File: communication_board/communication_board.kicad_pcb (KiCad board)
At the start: 2 copper layers, 23 parts, among them J1 Conn_01x04_Socket, J2 Conn_01x04_Socket, U1 FE1.1s, U2 FT232RL, Y1 Crystal

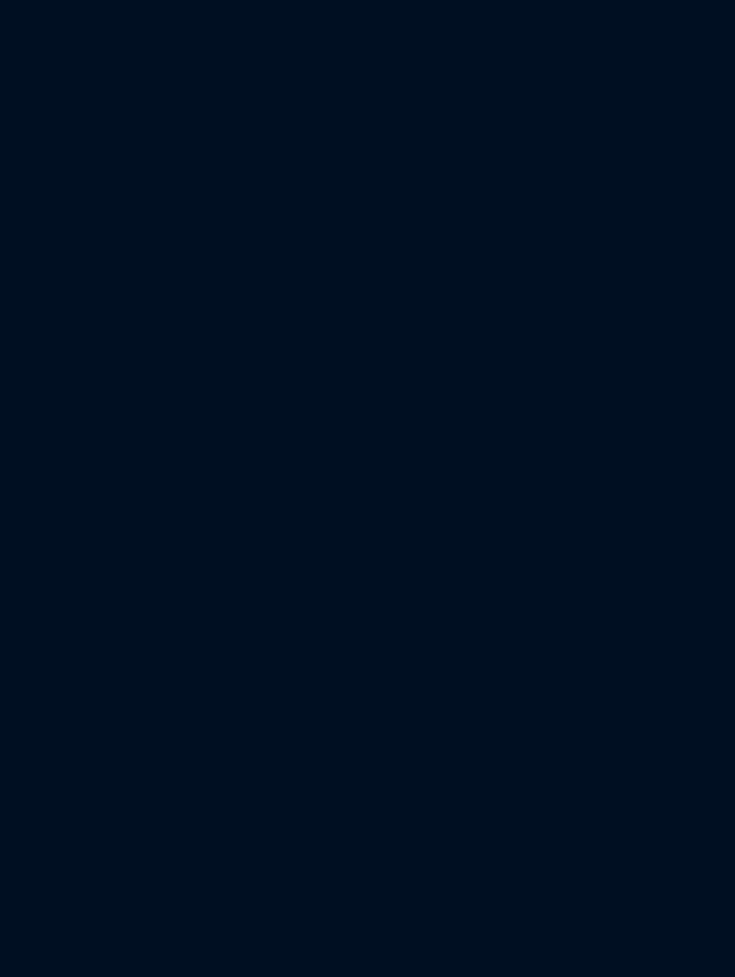
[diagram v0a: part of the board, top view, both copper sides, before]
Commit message: motors conversor almost ready for test
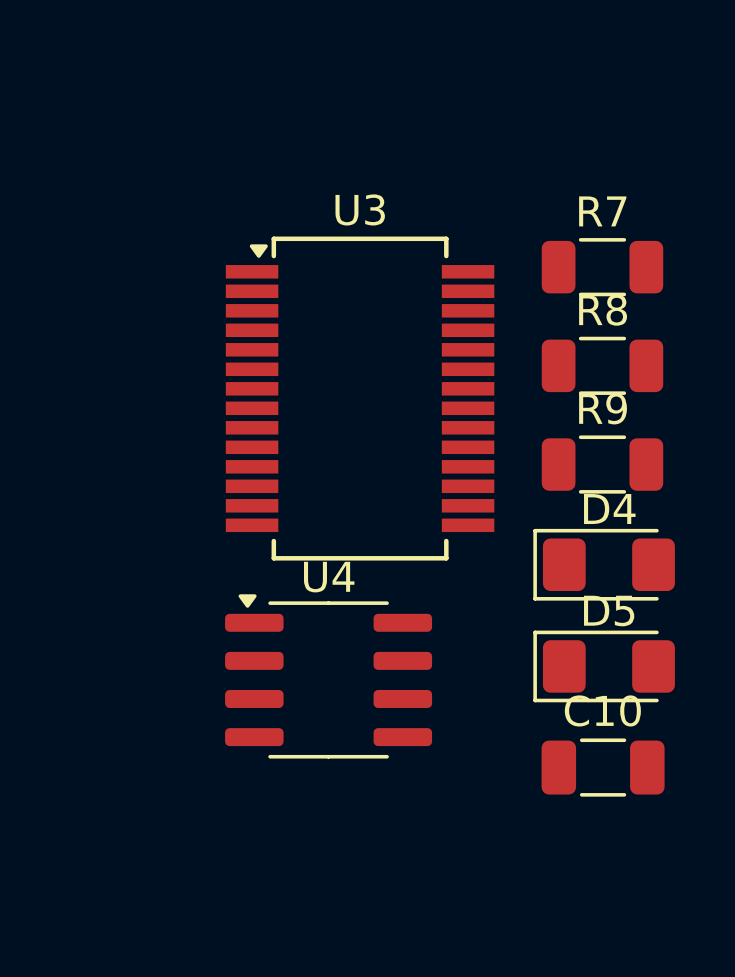
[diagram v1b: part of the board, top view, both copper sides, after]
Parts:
- added C10: 0.1uF, Capacitor_SMD:C_1206_3216Metric, F.Cu at (195.5, 76.5)
- added D4: IMU_TX, LED_SMD:LED_1206_3216Metric_Pad1.42x1.75mm_HandSolder, F.Cu at (195.7, 69.7)
- added D5: IMU_RX, LED_SMD:LED_1206_3216Metric_Pad1.42x1.75mm_HandSolder, F.Cu at (195.7, 73.1)
- added R7: 10K, Resistor_SMD:R_1206_3216Metric, F.Cu at (195.5, 59.8)
- added R8: 270, Resistor_SMD:R_1206_3216Metric, F.Cu at (195.5, 63.1)
- added R9: 270, Resistor_SMD:R_1206_3216Metric, F.Cu at (195.5, 66.4)
- added U3: FT232RL, Package_SO:SSOP-28_5.3x10.2mm_P0.65mm, F.Cu at (187.4, 64.2)
- added U4: MAX485E, Package_SO:SOIC-8_3.9x4.9mm_P1.27mm, F.Cu at (186.4, 73.6)
- R2: value 1K -> 330
- R3, R4: value 1k -> 330
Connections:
- net IMU_USB_D+_1 renamed IMU_USB_D+
- net IMU_USB_D-_1 renamed IMU_USB_D-
- U1 pad 8: HUB_USB_D-_2 -> MOTORS_USB_D-
- U1 pad 9: HUB_USB_D+_2 -> MOTORS_USB_D+
- U2 pad 22: unconnected-(U2-CBUS1-Pad22) -> Net-(D5-K)
- U2 pad 23: unconnected-(U2-CBUS0-Pad23) -> Net-(D4-K)

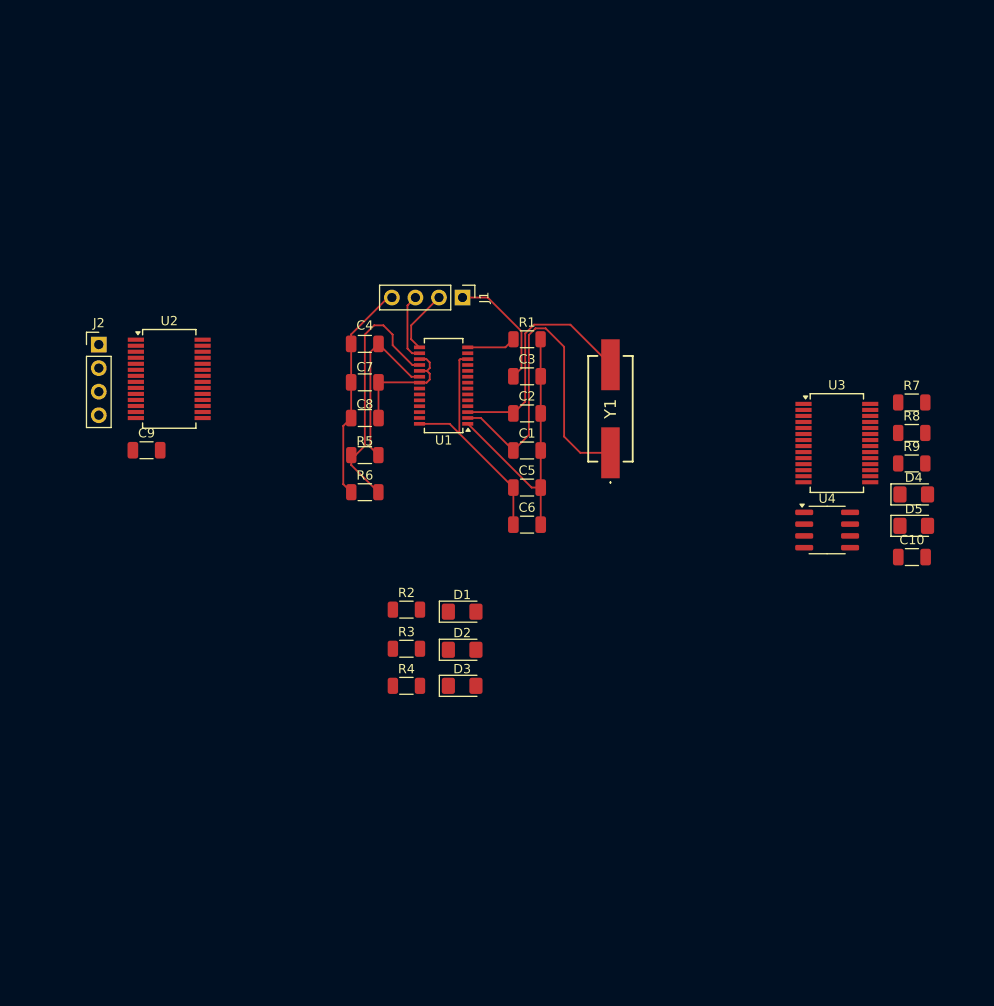
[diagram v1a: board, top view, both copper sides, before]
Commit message: initial pcd components disposition
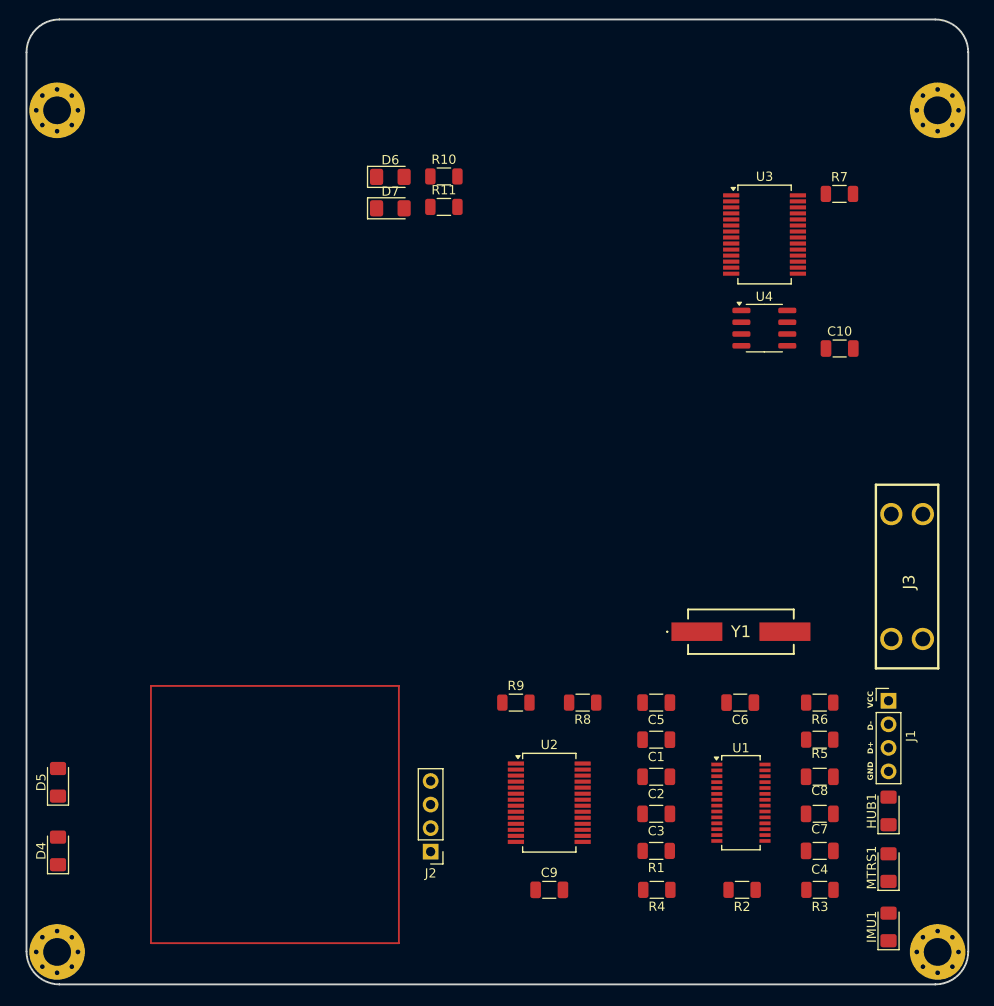
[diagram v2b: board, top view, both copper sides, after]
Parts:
- added D6: MTR_TX, LED_SMD:LED_1206_3216Metric_Pad1.42x1.75mm_HandSolder, F.Cu at (139.3, 35.5)
- added D7: MTR_RX, LED_SMD:LED_1206_3216Metric_Pad1.42x1.75mm_HandSolder, F.Cu at (139.3, 38.9)
- added J3: MINI_FUSE, humanoid:MINI_FUSE, F.Cu at (195.0, 78.6)
- added R10: 270, Resistor_SMD:R_1206_3216Metric, F.Cu at (145.0, 35.4)
- added R11: 270, Resistor_SMD:R_1206_3216Metric, F.Cu at (145.0, 38.7)
- added REF**: MountingHole_3mm_Pad_Via, MountingHole:MountingHole_3mm_Pad_Via, F.Cu at (198.3, 28.3)
- added REF**: MountingHole_3mm_Pad_Via, MountingHole:MountingHole_3mm_Pad_Via, F.Cu at (198.3, 119.1)
- added REF**: MountingHole_3mm_Pad_Via, MountingHole:MountingHole_3mm_Pad_Via, F.Cu at (103.3, 119.1)
- added REF**: MountingHole_3mm_Pad_Via, MountingHole:MountingHole_3mm_Pad_Via, F.Cu at (103.3, 28.3)
- J1: value Conn_01x04_Socket -> USB_IN
- J2: value Conn_01x04_Socket -> IMU
- moved D4 100.0 mm to (103.4, 108.2), turned to 90 degrees
- moved D5 96.4 mm to (103.4, 100.8), turned to 90 degrees
- moved C4 73.5 mm to (185.6, 108.2), turned to 0 degrees
- moved C7 67.6 mm to (185.6, 104.2), turned to 0 degrees
- moved J2 65.4 mm to (143.6, 108.3), turned to 180 degrees
- moved C9 64.3 mm to (156.4, 112.4)
- moved J1 63.3 mm to (193.0, 92.0), turned to 0 degrees
- moved C8 62.5 mm to (185.6, 100.2), turned to 0 degrees
- moved U2 61.4 mm to (156.4, 103.0)
- moved R5 57.9 mm to (185.6, 96.2), turned to 0 degrees
- moved IMU1 57.2 mm to (193.0, 116.4), turned to 90 degrees
- moved R1 56.9 mm to (167.9, 108.2), turned to 180 degrees
- moved U1 55.3 mm to (177.1, 103.0), turned to 0 degrees
- moved R6 54.1 mm to (185.6, 92.2), turned to 180 degrees
- moved MTRS1 51.7 mm to (193.0, 110.0), turned to 90 degrees
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- renumbered D3 to HUB1, D1 to IMU1, D2 to MTRS1
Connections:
- J1 pad 1: USB_PWR -> Net-(J1-Pin_1)
- U3 pad 22: unconnected-(U3-CBUS1-Pad22) -> Net-(D7-K)
- U3 pad 23: unconnected-(U3-CBUS0-Pad23) -> Net-(D6-K)
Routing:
- net GNDREF: track 54.5 -> 0.00 mm
- net Net-(U1-XOUT): track 39.9 -> 0.00 mm
- net USB_PWR: track 31.7 -> 0.00 mm
- net Net-(U1-VBUSM): track 27.8 -> 0.00 mm
- net Net-(U1-VD18): track 25.8 -> 0.00 mm
- net Net-(U1-XIN): track 25.5 -> 0.00 mm
- net 3v3: track 13.7 -> 0.00 mm
- net USB_D+: track 7.37 -> 0.00 mm
- net USB_D-: track 7.00 -> 0.00 mm
- net Net-(U1-REXT): track 5.30 -> 0.00 mm
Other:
- board outline added: 101.6 x 104.1 mm
- board text added: "D+"
- board text added: "D-"
- board text added: "GND"
- board text added: "VCC"

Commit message: start to track
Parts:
- moved HUB1 6.74 mm to (186.5, 105.7)
- moved MTRS1 6.58 mm to (186.5, 111.0)
- moved IMU1 6.50 mm to (186.5, 116.5)
- moved J1 6.50 mm to (186.5, 92.1)
- moved R4 5.56 mm to (162.4, 112.5)
- moved C1 5.50 mm to (162.4, 96.3)
- moved C2 5.50 mm to (162.4, 100.3)
- moved C3 5.50 mm to (162.4, 104.3)
- moved C4 5.50 mm to (180.1, 108.3)
- moved C5 5.50 mm to (162.4, 92.3)
- moved C6 5.50 mm to (171.5, 92.3)
- moved C7 5.50 mm to (180.1, 104.3)
- moved C8 5.50 mm to (180.1, 100.3)
- moved C9 5.50 mm to (150.9, 112.5)
- moved R1 5.50 mm to (162.4, 108.3)
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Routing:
- net GNDREF: track 0.00 -> 161.9 mm
- net USB_PWR: track 0.00 -> 109.4 mm, vias 0 -> 3
- net Net-(U1-VD18): track 0.00 -> 61.9 mm, vias 0 -> 2
- net Net-(HUB1-K): track 0.00 -> 50.3 mm
- net 3v3: track 0.00 -> 37.2 mm
- net Net-(U1-VBUSM): track 0.00 -> 37.2 mm
- net USB_D-: track 0.00 -> 36.5 mm
- net USB_D+: track 0.00 -> 33.6 mm
- net IMU_USB_D-: track 0.00 -> 27.9 mm
- net Net-(HUB1-A): track 0.00 -> 27.9 mm, vias 0 -> 2
- net IMU_USB_D+: track 0.00 -> 27.7 mm
- net Net-(U1-XIN): track 0.00 -> 24.1 mm
- net Net-(IMU1-K): track 0.00 -> 18.5 mm
- net Net-(U1-XOUT): track 0.00 -> 18.1 mm
- net Net-(U1-LED2): track 0.00 -> 15.4 mm
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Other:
- outline, holes or cut-outs redrawn

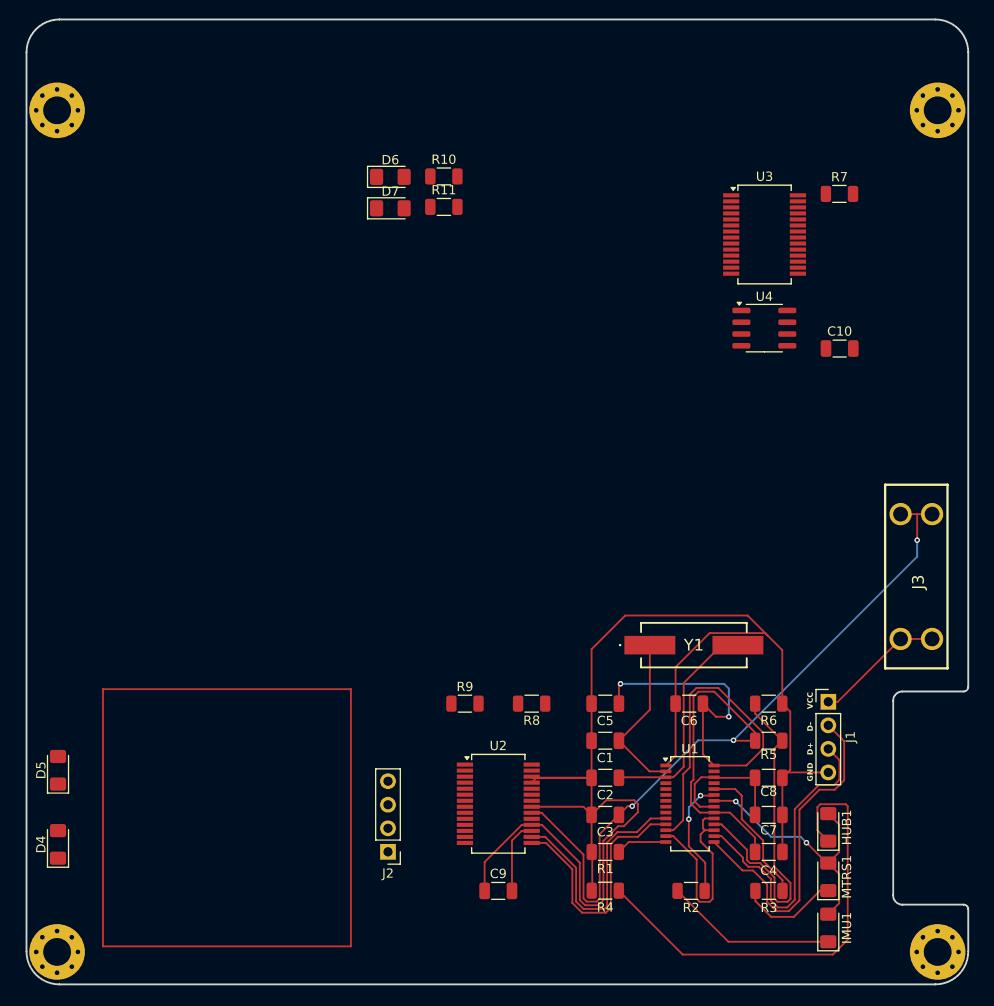
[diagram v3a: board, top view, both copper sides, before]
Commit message: board cut ajusted
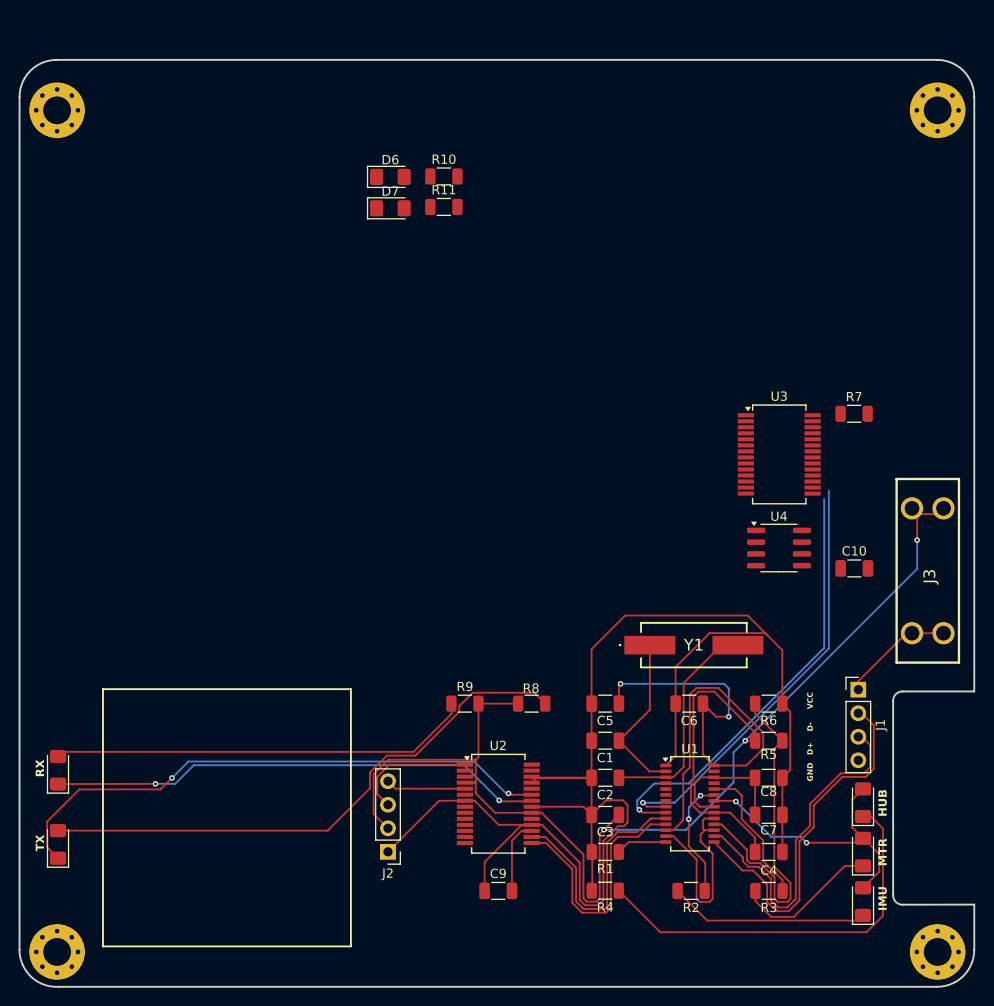
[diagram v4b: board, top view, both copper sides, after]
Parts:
- moved C10 23.8 mm to (189.3, 77.7)
- moved U3 23.8 mm to (181.2, 65.4)
- moved U4 23.8 mm to (181.2, 75.5)
- moved R7 23.8 mm to (189.3, 61.0)
- moved IMU1 4.71 mm to (190.2, 113.7)
- moved HUB1 4.60 mm to (190.2, 103.0)
- moved MTRS1 4.60 mm to (190.2, 108.3)
- moved J1 3.49 mm to (189.7, 90.8)
- moved J3 1.38 mm to (197.2, 78.0)
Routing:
- net Net-(D4-K): track 0.00 -> 60.9 mm, vias 0 -> 2
- net Net-(D4-A): track 0.00 -> 60.6 mm
- net Net-(D5-K): track 0.00 -> 53.6 mm, vias 0 -> 2
- net MOTORS_USB_D+: track 0.00 -> 47.1 mm, vias 0 -> 1
- net MOTORS_USB_D-: track 0.00 -> 46.6 mm, vias 0 -> 1
- net USB_PWR: track 109.4 -> 154.9 mm
- net Net-(D5-A): track 0.00 -> 45.5 mm
- net Net-(J2-Pin_3): track 0.00 -> 13.5 mm
- net GNDREF: track 161.9 -> 174.7 mm
- net Net-(J2-Pin_4): track 0.00 -> 8.63 mm
- net Net-(HUB1-K): track 50.3 -> 43.2 mm
- net Net-(MTRS1-K): track 10.8 -> 15.7 mm
- net USB_D+: track 33.6 -> 37.0 mm
- net Net-(HUB1-A): track 27.9 -> 31.3 mm
- net USB_D-: track 36.5 -> 39.8 mm
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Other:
- board size 101.6 x 104.1 mm -> 103 x 100 mm
- board text added: "HUB"
- board text added: "IMU"
- board text added: "MTR"
- board text added: "RX"
- board text added: "TX"

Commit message: communication board finished
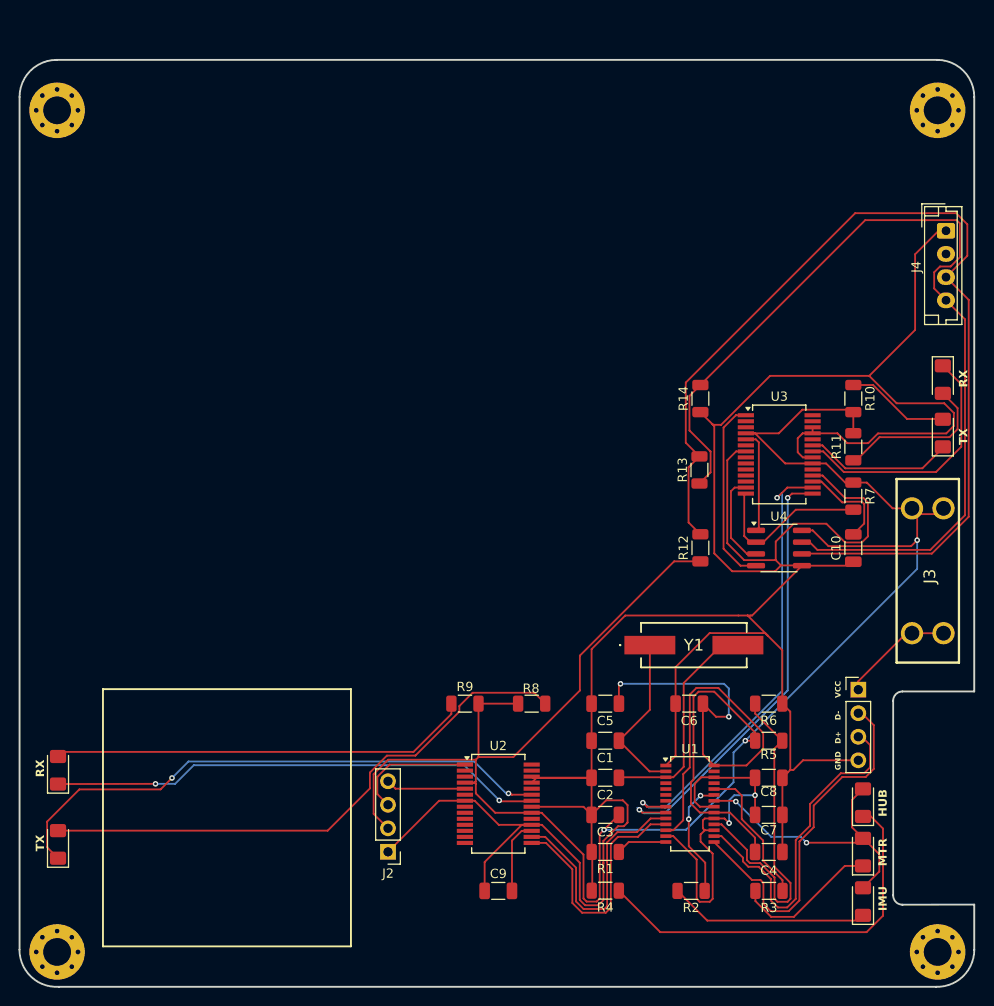
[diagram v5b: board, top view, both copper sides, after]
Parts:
- added J4: Motors, Connector_JST:JST_EH_B4B-EH-A_1x04_P2.50mm_Vertical, F.Cu at (199.2, 41.3)
- added R12: 680, Resistor_SMD:R_1206_3216Metric, F.Cu at (172.7, 75.5)
- added R13: 120, Resistor_SMD:R_1206_3216Metric, F.Cu at (172.6, 67.1)
- added R14: 680, Resistor_SMD:R_1206_3216Metric, F.Cu at (172.7, 59.4)
- moved D6 65.7 mm to (198.9, 63.1), turned to 90 degrees
- moved D7 62.4 mm to (198.9, 57.4), turned to -90 degrees
- moved R11 51.2 mm to (189.2, 64.6), turned to 90 degrees
- moved R10 50.3 mm to (189.2, 59.4), turned to -90 degrees
- moved R7 8.88 mm to (189.2, 69.9), turned to -90 degrees
- moved C10 2.20 mm to (189.2, 75.5), turned to 90 degrees
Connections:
- U4 pad 6: unconnected-(U4-A-Pad6) -> Net-(U4-A)
- U4 pad 7: unconnected-(U4-B-Pad7) -> Net-(U4-B)
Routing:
- net GNDREF: track 174.7 -> 338.7 mm
- net Net-(U4-A): track 0.00 -> 109.6 mm
- net Net-(U4-B): track 0.00 -> 102.2 mm
- net USB_PWR: track 154.9 -> 239.5 mm
- net Net-(D7-K): track 0.00 -> 27.7 mm
- net Net-(U3-TXD): track 0.00 -> 20.3 mm
- net Net-(U3-CBUS3): track 0.00 -> 18.1 mm
- net Net-(D7-A): track 0.00 -> 17.2 mm
- net Net-(D6-K): track 0.00 -> 16.1 mm
- net Net-(D6-A): track 0.00 -> 11.2 mm
- net Net-(U3-RXD): track 0.00 -> 11.2 mm
- net Net-(U3-3V3OUT): track 0.00 -> 10.4 mm
- net Net-(U3-CBUS2): track 0.00 -> 10.2 mm
- net 3v3: track 37.2 -> 44.5 mm, vias 0 -> 2
- net MOTORS_USB_D-: track 46.6 -> 49.5 mm, vias 1 -> 2
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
